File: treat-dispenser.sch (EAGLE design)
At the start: 32 parts, among them U1 MCP73831, U2 TPS6103x, Y1 16MHz

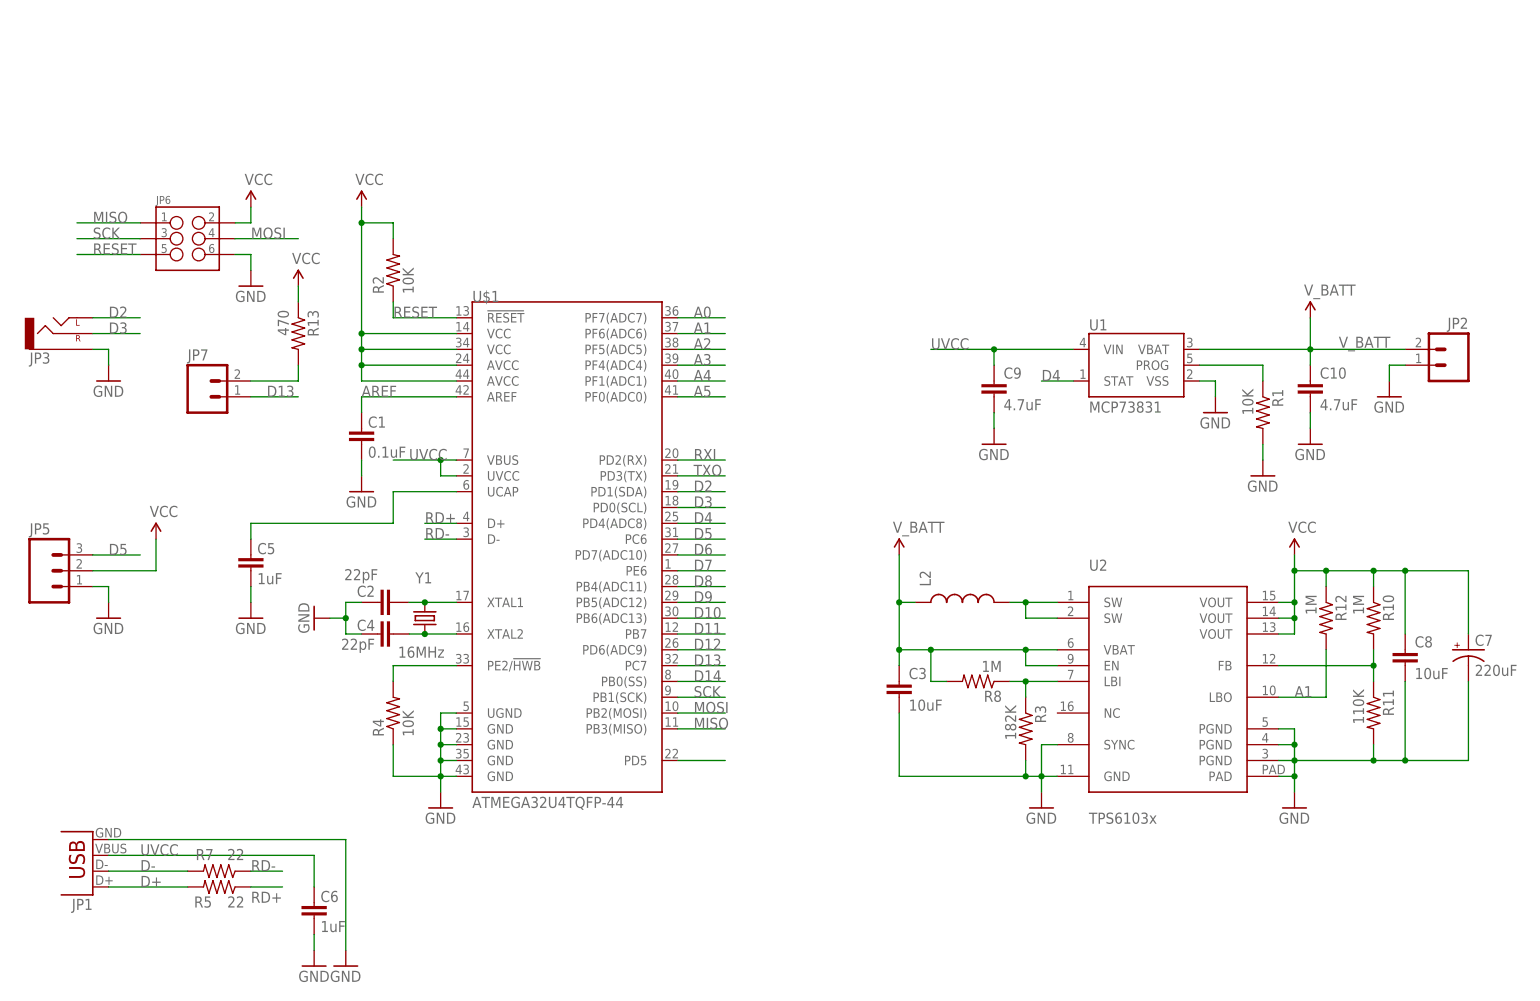
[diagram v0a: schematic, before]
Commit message: moved servo to clear path for battery connector
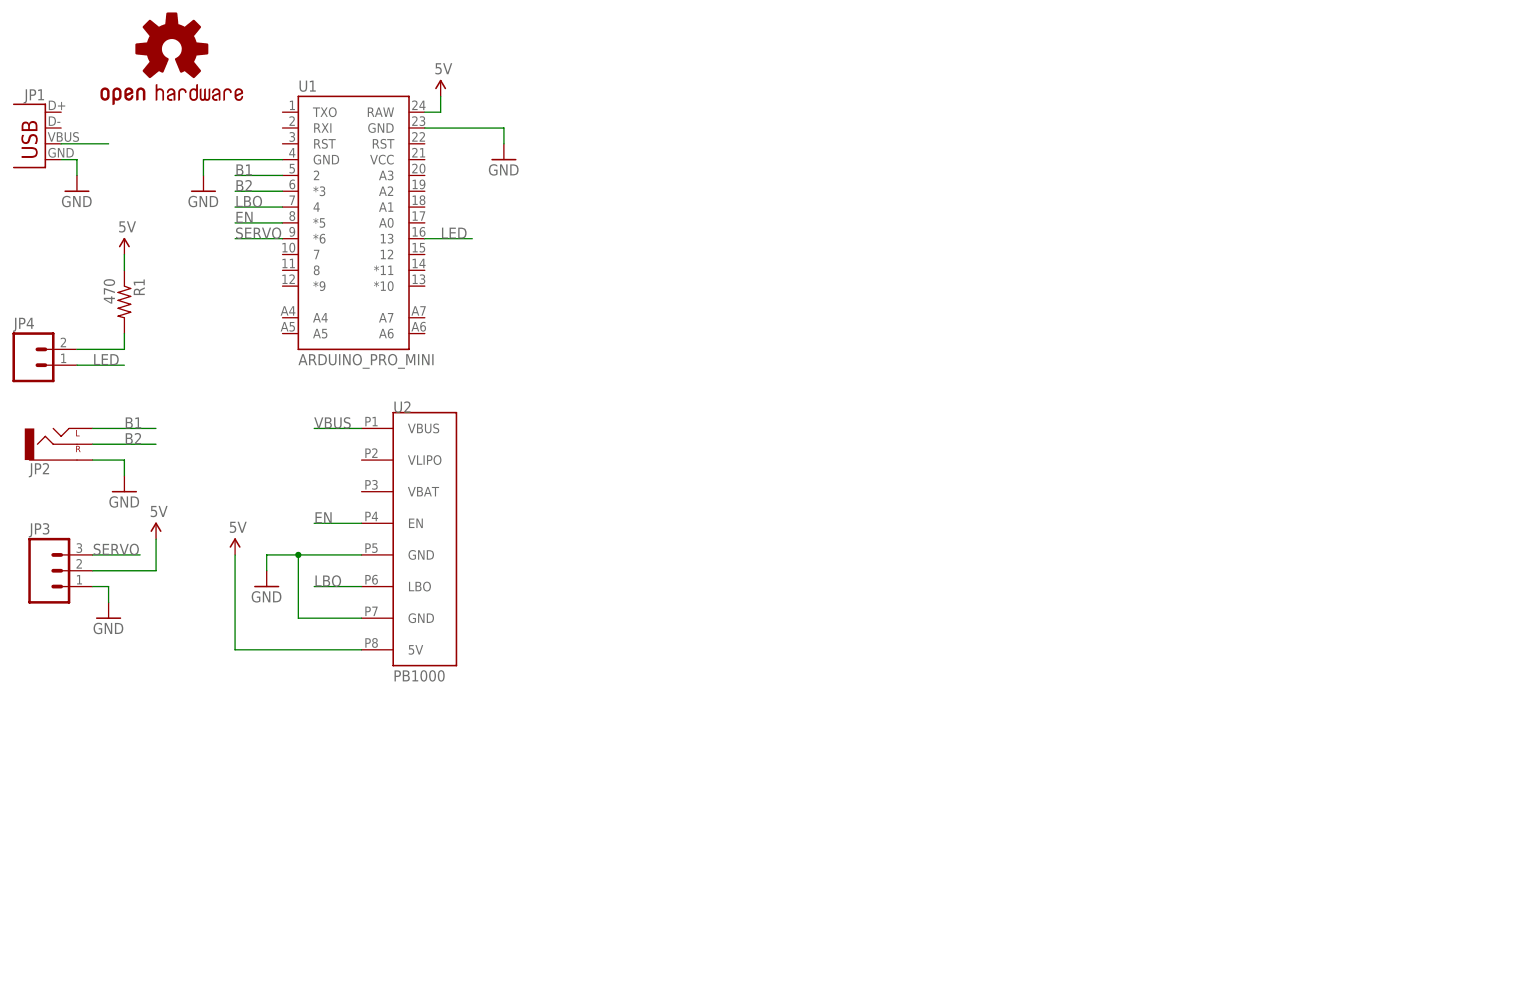
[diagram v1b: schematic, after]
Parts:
- removed C1: 0.1uF, SparkFun:CAP0603-CAP
- removed C10, C9: 4.7uF, SparkFun:CAP0603-CAP
- removed C2, C4: 22pF, SparkFun:CAP0603-CAP
- removed C3, C8: 10uF, SparkFun:CAP0603-CAP
- removed C5, C6: 1uF, SparkFun:CAP0603-CAP
- removed C7: 220uF, SparkFun-Capacitors:CAP_POLPTH1
- removed JP5: (no value), SparkFun-Connectors:M03PTH
- removed JP6: (no value), SparkFun-Connectors:M03X2FEMALE
- removed JP7: (no value), SparkFun-Connectors:M02PTH
- removed L2: (no value), SparkFun-Passives:INDUCTOR
- removed R10, R12, R8: 1M, SparkFun:RESISTOR0603-RES
- removed R11: 110K, SparkFun:RESISTOR0603-RES
- removed R13: 470, SparkFun:RESISTOR0603-RES
- removed R2, R4: 10K, SparkFun:RESISTOR0603-RES
- removed R3: 182K, SparkFun:RESISTOR0603-RES
- removed R5, R7: 22, SparkFun:RESISTOR0603-RES
- removed U$1: ATMEGA32U4TQFP-44, SparkFun-DigitalIC:ATMEGA32U4TQFP-44
- removed Y1: 16MHz, SparkFun:CRYSTALHC49US
- added JP4: (no value), SparkFun-Connectors:M02PTH
- added LOGO1: OSHW-LOGOS, SparkFun-Aesthetics:OSHW-LOGOS
- JP2: device SparkFun-Connectors:M02JST-PTH-2-KIT -> SparkFun-Connectors:AUDIO-JACKPTH; PN S2B-PH-K-S(LF)(SN) -> CP1-3523N-ND
- JP3: device SparkFun-Connectors:AUDIO-JACKPTH -> SparkFun-Connectors:M03PTH; PN SJ1-3523N -> 952-1312-ND
- R1: value 10K -> 470; device SparkFun:RESISTOR0603-RES -> SparkFun:RESISTORPTH-1/4W; PN CR0603-JW-103ELF -> CF14JT470RCT-ND
- U1: value MCP73831 -> ARDUINO_PRO_MINI; device SparkFun:MCP73831 -> SparkFun-Boards:ARDUINO_PRO_MINI; PN MCP73831T-2ATI/OT -> 1568-1055-ND
- U2: value TPS6103x -> PB1000; device tps6103x:TPS6103X -> powerboost:PB1000; PN TPS61032PWPR -> 1528-1349-ND
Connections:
- removed net A0: U$1.PF7(ADC7)
- removed net A1: R12.2, U$1.PF6(ADC6), U2.LBO
- removed net A2: U$1.PF5(ADC5)
- removed net A3: U$1.PF4(ADC4)
- removed net A4: U$1.PF1(ADC1)
- removed net A5: U$1.PF0(ADC0)
- removed net AREF: C1.2, U$1.AREF
- removed net D+: JP1.D+, R5.2
- removed net D-: JP1.D-, R7.2
- removed net D10: U$1.PB6(ADC13)
- removed net D11: U$1.PB7
- removed net D12: U$1.PD6(ADC9)
- removed net D13: JP7.1, U$1.PC7
- removed net D14: U$1.PB0(SS)
- removed net D2: JP3.LEFT, U$1.PD1(SDA)
- removed net D3: JP3.RIGHT, U$1.PD0(SCL)
- removed net D4: U$1.PD4(ADC8), U1.STAT
- removed net D5: JP5.3, U$1.PC6
- removed net D6: U$1.PD7(ADC10)
- removed net D7: U$1.PE6
- removed net D8: U$1.PB4(ADC11)
- removed net D9: U$1.PB5(ADC12)
- removed net FB: R10.2, R11.1, U2.FB
- removed net LBI: R3.1, R8.1, U2.LBI
- removed net MISO: JP6.1, U$1.PB3(MISO)
- removed net MOSI: JP6.4, U$1.PB2(MOSI)
- removed net N$1: C4.1, U$1.XTAL2, Y1.1
- removed net N$2: C2.1, U$1.XTAL1, Y1.2
- removed net N$3: U$1.PD5
- removed net N$4: C5.2, U$1.UCAP
- removed net N$5: R4.2, U$1.PE2/!HWB
- removed net PROG: R1.1, U1.PROG
- removed net RD+: R5.1, U$1.D+
- removed net RD-: R7.1, U$1.D-
- removed net RESET: JP6.5, R2.1, U$1.!RESET
- removed net RXI: U$1.PD2(RX)
- removed net SCK: JP6.3, U$1.PB1(SCK)
- removed net SW: L2.2, U2.SW@1, U2.SW@2
- removed net TXO: U$1.PD3(TX)
- removed net UVCC: C6.2, C9.1, JP1.VBUS, U$1.UVCC, U$1.VBUS, U1.VIN
- removed net VCC: C7.+, C8.1, JP5.2, JP6.2, R10.1, R12.1, R13.1, R2.2, U$1.AVCC@24, U$1.AVCC@44, U$1.VCC@14, U$1.VCC@34, U2.VOUT@13, U2.VOUT@14, U2.VOUT@15
- removed net V_BATT: C10.1, C3.1, JP2.2, L2.1, R8.2, U1.VBAT, U2.EN, U2.VBAT
- new net 5V: JP3.2, R1.1, U1.RAW, U2.5V
- new net B1: JP2.LEFT, U1.2
- new net B2: JP2.RIGHT, U1.*3
- new net EN: U1.*5, U2.EN
- new net LBO: U1.4, U2.LBO
- new net LED: JP4.1, U1.13
- new net SERVO: JP3.3, U1.*6
- new net VBUS: JP1.VBUS, U2.VBUS
- net GND: now also JP2.SLEEVE, JP3.1, U1.GND, U1.GND@2, U2.GND@5, U2.GND@7; no longer C1.1, C10.2, C2.2, C3.2, C4.2, C5.1, C6.1, C7.-, C8.2, C9.2, JP2.1, JP3.SLEEVE, JP5.1, JP6.6, R1.2, R11.2, R3.2, R4.1, U$1.GND@15, U$1.GND@23, U$1.GND@35, U$1.GND@43, U$1.UGND, U1.VSS, U2.GND, U2.PAD, U2.PGND@3, U2.PGND@4, U2.PGND@5, U2.SYNC
- net N$8: now also JP4.2, R1.2; no longer JP7.2, R13.2
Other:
- moved on the sheet: JP1, JP3, R1

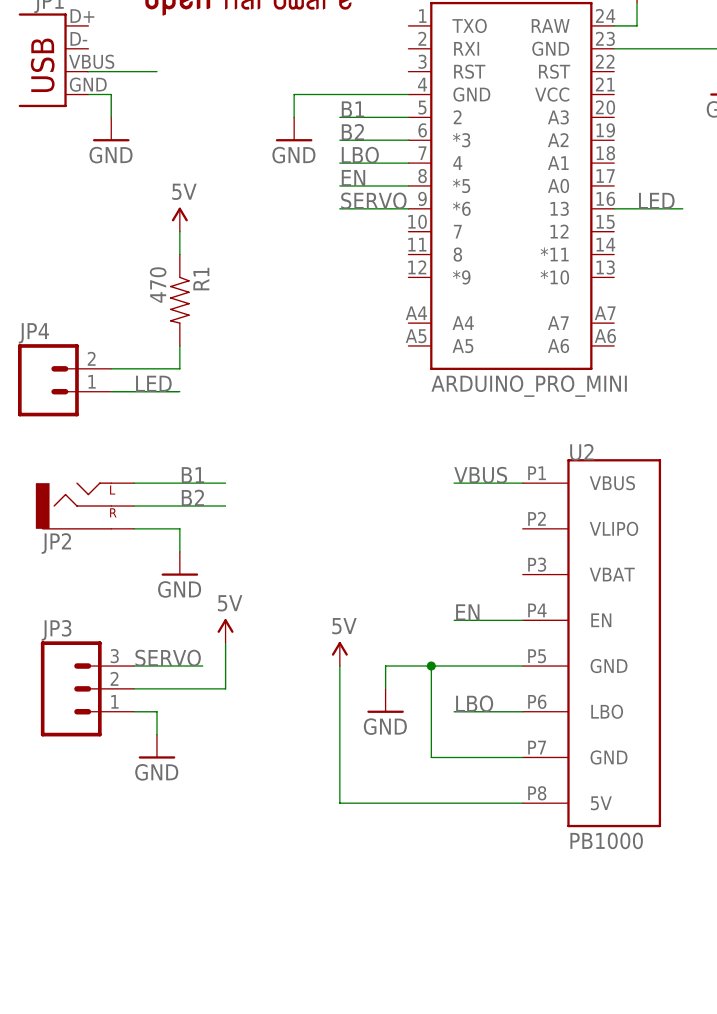
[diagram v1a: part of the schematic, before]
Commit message: rev C update: - added dedicated battery connector - reversed led polarity - added enable switch - removed en connection to arduino - added status led and lbo to arduino code
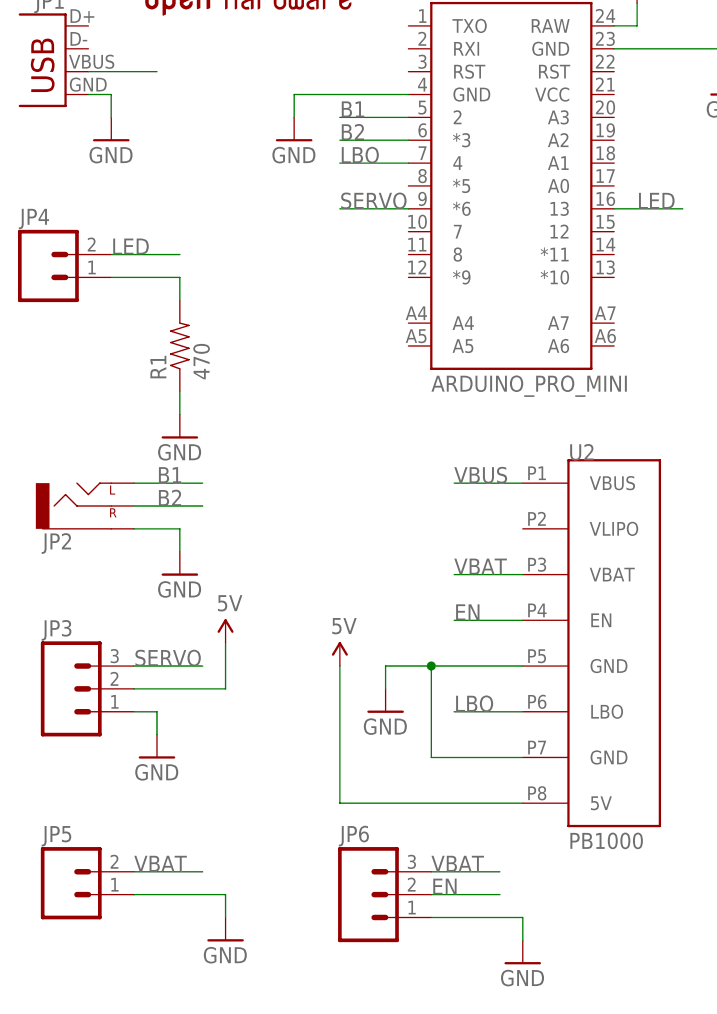
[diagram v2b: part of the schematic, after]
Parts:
- added JP5: (no value), SparkFun-Connectors:M02JST-PTH-2
- added JP6: (no value), SparkFun-Connectors:M03PTH
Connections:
- removed net N$8: JP4.2, R1.2
- new net N$5: JP4.1, R1.2
- new net VBAT: JP5.2, JP6.3, U2.VBAT
- net 5V: no longer R1.1
- net EN: now also JP6.2; no longer U1.*5
- net GND: now also JP5.1, JP6.1, R1.1
- net LED: now also JP4.2; no longer JP4.1
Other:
- moved on the sheet: JP4, R1
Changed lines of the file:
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@@
 <part name="SUPPLY2" library="SparkFun-Aesthetics" deviceset="5V" device=""/>
 <part name="GND3" library="supply1" deviceset="GND" device=""/>
-<part name="SUPPLY3" library="SparkFun-Aesthetics" deviceset="5V" device=""/>
 <part name="JP1" library="SparkFun-Connectors" deviceset="USB" device="-MB-H" value="">
 <attribute name="PN" value="WM17115-ND"/>
@@
 <part name="SUPPLY4" library="SparkFun-Aesthetics" deviceset="5V" device=""/>
 <part name="LOGO1" library="SparkFun-Aesthetics" deviceset="OSHW-LOGO" device="S"/>
+<part name="JP5" library="SparkFun-Connectors" deviceset="M02" device="JST-PTH-2">
+<attribute name="PN" value="455-1719-ND"/>
+</part>
+<part name="GND5" library="supply1" deviceset="GND" device=""/>
+<part name="JP6" library="SparkFun-Connectors" deviceset="M03" device="PTH">
+<attribute name="PN" value="EG1903-ND"/>
+</part>
+<part name="GND6" library="supply1" deviceset="GND" device=""/>
+<part name="GND7" library="supply1" deviceset="GND" device=""/>
 </parts>
 <sheets>
@@
 <instance part="GND10" gate="1" x="20.32" y="99.06"/>
 <instance part="GND12" gate="1" x="22.86" y="119.38"/>
-<instance part="JP4" gate="G$1" x="7.62" y="139.7">
-<attribute name="PN" x="7.62" y="139.7" size="1.778" layer="96" display="off"/>
-</instance>
-<instance part="R1" gate="G$1" x="22.86" y="149.86" rot="R270">
-<attribute name="PN" x="22.86" y="149.86" size="1.778" layer="96" rot="R270" display="off"/>
+<instance part="JP4" gate="G$1" x="7.62" y="152.4">
+<attribute name="PN" x="7.62" y="152.4" size="1.778" layer="96" display="off"/>
+</instance>
+<instance part="R1" gate="G$1" x="22.86" y="144.78" rot="R90">
+<attribute name="PN" x="22.86" y="144.78" size="1.778" layer="96" rot="R90" display="off"/>
 </instance>
 <instance part="U1" gate="G$1" x="58.42" y="165.1">
@@
 <instance part="SUPPLY2" gate="G$1" x="40.64" y="109.22"/>
 <instance part="GND3" gate="1" x="45.72" y="104.14"/>
-<instance part="SUPPLY3" gate="G$1" x="22.86" y="157.48"/>
 <instance part="JP1" gate="G$1" x="10.16" y="172.72" rot="MR0">
 <attribute name="PN" x="10.16" y="172.72" size="1.778" layer="96" rot="MR0" display="off"/>
@@
 <instance part="SUPPLY4" gate="G$1" x="73.66" y="182.88"/>
 <instance part="LOGO1" gate="G$1" x="30.48" y="190.5"/>
+<instance part="JP5" gate="G$1" x="10.16" y="83.82">
+<attribute name="PN" x="10.16" y="83.82" size="1.778" layer="96" display="off"/>
+</instance>
+<instance part="GND5" gate="1" x="27.94" y="78.74"/>
+<instance part="JP6" gate="G$1" x="43.18" y="83.82">
+<attribute name="PN" x="43.18" y="83.82" size="1.778" layer="96" display="off"/>
+</instance>
+<instance part="GND6" gate="1" x="60.96" y="76.2"/>
+<instance part="GND7" gate="1" x="22.86" y="134.62"/>
 </instances>
 <busses>
@@
 <wire x1="15.24" y1="172.72" x2="15.24" y2="170.18" width="0.1524" layer="91"/>
 </segment>
+<segment>
+<pinref part="R1" gate="G$1" pin="1"/>
+<wire x1="22.86" y1="139.7" x2="22.86" y2="137.16" width="0.1524" layer="91"/>
+<pinref part="GND7" gate="1" pin="GND"/>
+</segment>
+<segment>
+<pinref part="JP5" gate="G$1" pin="1"/>
+<pinref part="GND5" gate="1" pin="GND"/>
+<wire x1="17.78" y1="83.82" x2="27.94" y2="83.82" width="0.1524" layer="91"/>
+<wire x1="27.94" y1="83.82" x2="27.94" y2="81.28" width="0.1524" layer="91"/>
+</segment>
+<segment>
+<pinref part="JP6" gate="G$1" pin="1"/>
+<pinref part="GND6" gate="1" pin="GND"/>
+<wire x1="50.8" y1="81.28" x2="60.96" y2="81.28" width="0.1524" layer="91"/>
+<wire x1="60.96" y1="81.28" x2="60.96" y2="78.74" width="0.1524" layer="91"/>
+</segment>
 </net>
 <net name="SERVO" class="0">
@@
 <wire x1="48.26" y1="160.02" x2="40.64" y2="160.02" width="0.1524" layer="91"/>
 <label x="40.64" y="160.02" size="1.778" layer="95"/>
-</segment>
-</net>
-<net name="N$8" class="0">
-<segment>
-<pinref part="R1" gate="G$1" pin="2"/>
-<wire x1="22.86" y1="144.78" x2="22.86" y2="142.24" width="0.1524" layer="91"/>
-<pinref part="JP4" gate="G$1" pin="2"/>
-<wire x1="22.86" y1="142.24" x2="15.24" y2="142.24" width="0.1524" layer="91"/>
 </segment>
 </net>
@@
 </segment>
 <segment>
-<pinref part="R1" gate="G$1" pin="1"/>
-<wire x1="22.86" y1="154.94" x2="22.86" y2="157.48" width="0.1524" layer="91"/>
-<pinref part="SUPPLY3" gate="G$1" pin="5V"/>
-</segment>
-<segment>
 <pinref part="U1" gate="G$1" pin="RAW"/>
 <pinref part="SUPPLY4" gate="G$1" pin="5V"/>
@@
 <segment>
 <pinref part="JP2" gate="G$1" pin="RIGHT"/>
-<wire x1="17.78" y1="127" x2="27.94" y2="127" width="0.1524" layer="91"/>
-<label x="22.86" y="127" size="1.778" layer="95"/>
+<wire x1="17.78" y1="127" x2="25.4" y2="127" width="0.1524" layer="91"/>
+<label x="20.32" y="127" size="1.778" layer="95"/>
 </segment>
 <segment>
@@
 <net name="LED" class="0">
 <segment>
-<pinref part="JP4" gate="G$1" pin="1"/>
-<wire x1="15.24" y1="139.7" x2="22.86" y2="139.7" width="0.1524" layer="91"/>
-<label x="17.78" y="139.7" size="1.778" layer="95"/>
-</segment>
-<segment>
 <pinref part="U1" gate="G$1" pin="13"/>
 <wire x1="71.12" y1="160.02" x2="78.74" y2="160.02" width="0.1524" layer="91"/>
 <label x="73.66" y="160.02" size="1.778" layer="95"/>
 </segment>
+<segment>
+<pinref part="JP4" gate="G$1" pin="2"/>
+<wire x1="15.24" y1="154.94" x2="22.86" y2="154.94" width="0.1524" layer="91"/>
+<label x="15.24" y="154.94" size="1.778" layer="95"/>
+</segment>
 </net>
 <net name="B1" class="0">
 <segment>
 <pinref part="JP2" gate="G$1" pin="LEFT"/>
-<wire x1="17.78" y1="129.54" x2="27.94" y2="129.54" width="0.1524" layer="91"/>
-<label x="22.86" y="129.54" size="1.778" layer="95"/>
+<wire x1="17.78" y1="129.54" x2="25.4" y2="129.54" width="0.1524" layer="91"/>
+<label x="20.32" y="129.54" size="1.778" layer="95"/>
 </segment>
 <segment>
@@
 </segment>
 </net>
-<net name="EN" class="0">
-<segment>
-<wire x1="60.96" y1="114.3" x2="53.34" y2="114.3" width="0.1524" layer="91"/>
-<pinref part="U2" gate="G$1" pin="EN"/>
-<label x="53.34" y="114.3" size="1.778" layer="95"/>
-</segment>
-<segment>
-<pinref part="U1" gate="G$1" pin="*5"/>
-<wire x1="48.26" y1="162.56" x2="40.64" y2="162.56" width="0.1524" layer="91"/>
-<label x="40.64" y="162.56" size="1.778" layer="95"/>
+<net name="VBAT" class="0">
+<segment>
+<pinref part="U2" gate="G$1" pin="VBAT"/>
+<wire x1="53.34" y1="119.38" x2="60.96" y2="119.38" width="0.1524" layer="91"/>
+<label x="53.34" y="119.38" size="1.778" layer="95"/>
+</segment>
+<segment>
+<pinref part="JP5" gate="G$1" pin="2"/>
+<wire x1="17.78" y1="86.36" x2="25.4" y2="86.36" width="0.1524" layer="91"/>
+<label x="17.78" y="86.36" size="1.778" layer="95"/>
+</segment>
+<segment>
+<pinref part="JP6" gate="G$1" pin="3"/>
+<wire x1="50.8" y1="86.36" x2="58.42" y2="86.36" width="0.1524" layer="91"/>
+<label x="50.8" y="86.36" size="1.778" layer="95"/>
 </segment>
 </net>
@@
 </segment>
 </net>
+<net name="EN" class="0">
+<segment>
+<pinref part="U2" gate="G$1" pin="EN"/>
+<wire x1="60.96" y1="114.3" x2="53.34" y2="114.3" width="0.1524" layer="91"/>
+<label x="53.34" y="114.3" size="1.778" layer="95"/>
+</segment>
+<segment>
+<wire x1="50.8" y1="83.82" x2="58.42" y2="83.82" width="0.1524" layer="91"/>
+<pinref part="JP6" gate="G$1" pin="2"/>
+<label x="50.8" y="83.82" size="1.778" layer="95"/>
+</segment>
+</net>
+<net name="N$5" class="0">
+<segment>
+<pinref part="R1" gate="G$1" pin="2"/>
+<pinref part="JP4" gate="G$1" pin="1"/>
+<wire x1="15.24" y1="152.4" x2="22.86" y2="152.4" width="0.1524" layer="91"/>
+<wire x1="22.86" y1="152.4" x2="22.86" y2="149.86" width="0.1524" layer="91"/>
+</segment>
+</net>
